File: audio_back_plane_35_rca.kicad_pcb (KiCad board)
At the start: 4 copper layers, 75 x 61 mm, 30 parts, among them SW3 SW1, U1 ESP32-DevKitC - DEVKIT, U3 Teensy 4.1 - DEVKIT

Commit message: update
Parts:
- added C1: 0.1uF, project_fp:C_0805_2012Metric_Pad1.15x1.40mm_HandSolder, F.Cu at (103.2, 104.7)
- added C2: 0.1uF, project_fp:C_0805_2012Metric_Pad1.15x1.40mm_HandSolder, F.Cu at (118.3, 130.1)
- added C8: 1uF, project_fp:C_0805_2012Metric_Pad1.15x1.40mm_HandSolder, F.Cu at (109.1, 129.9)
- added D3: SK6812_4020_SIDE_LED, project_fp:LED_4691, F.Cu at (107.2, 100.2)
- added D4: SK6812_4020_SIDE_LED, project_fp:LED_4691, F.Cu at (119.5, 100.2)
- added R1: 2.2k ohm - 2200 ohm, project_fp:R_0805_2012Metric_Pad1.20x1.40mm_HandSolder, F.Cu at (117.2, 125.1)
- D1, D2: value WS2812B - COM-16347 -> HEADER; footprint Connector_PinHeader_1.00mm:PinHeader_1x04_P1.00mm_Vertical -> project_fp:PinHeader_1x04_P1.00mm_Vertical_WS2812_LED_mod
- R10, R12, R13, R14, R17, R19, R20, R21, R6, R7, R8, R9: footprint Resistor_THT:R_Axial_DIN0204_L3.6mm_D1.6mm_P5.08mm_Horizontal -> project_fp:R_0805_2012Metric_Pad1.20x1.40mm_HandSolder
- SW3: value SW1 -> OS102011MA1QN1
- board_outline1: value board -> TAC5212 Module
- moved board_outline2 30.0 mm to (98.5, 146.7)
- moved G1 14.0 mm to (113.5, 130.1), turned to 0 degrees
- moved R12 7.47 mm to (134.9, 105.1)
- moved C3 4.54 mm to (109.0, 111.9), turned to -90 degrees
- moved C5 4.44 mm to (118.5, 111.9), turned to -90 degrees
- moved R8 3.54 mm to (134.3, 132.5)
- moved R19 3.16 mm to (164.5, 98.5)
- moved R20 3.16 mm to (161.4, 98.5)
- moved R21 3.16 mm to (158.2, 98.5)
- moved R14 2.54 mm to (134.9, 107.7)
- moved D2 2.30 mm to (118.0, 108.3)
- moved D1 2.20 mm to (106.0, 108.3)
- moved R17 1.55 mm to (116.2, 111.9), turned to -90 degrees
- moved R10 1.54 mm to (134.3, 127.7)
- moved R9 1.54 mm to (134.3, 130.1)
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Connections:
- HPTRS1 pad 2: Net-(board_outline1-OUTP) -> Net-(board_outline1-OUT2P)
- HPTRS1 pad 5: Net-(board_outline1-OUT2P) -> Net-(board_outline1-OUTP)
- HPTRS2 pad 2: Net-(board_outline1-IN1P) -> Net-(SW3-C)
- HPTRS2 pad 5: Net-(SW3-C) -> Net-(board_outline1-IN1P)
- MIC1 pad 2: unconnected-(MIC1-SELECT-Pad2) -> GND
- MIC2 pad 2: unconnected-(MIC2-SELECT-Pad2) -> 3.3V
- U1 pad 23: Net-(ILI1-CS) -> unconnected-(U1-*MTDO/GPIO15/ADC2_CH3-Pad23)
- U1 pad 24: Net-(ILI1-DC) -> unconnected-(U1-ADC2_CH2/*GPIO2-Pad24)
- U1 pad 26: Net-(ILI1-RESET) -> unconnected-(U1-ADC2_CH0/GPIO4-Pad26)
- U1 pad 30: Net-(ILI1-SCK) -> unconnected-(U1-GPIO18-Pad30)
- U1 pad 31: Net-(ILI1-T_DO(MISO)) -> unconnected-(U1-GPIO19-Pad31)
- U1 pad 33: /ESP32_IO21_SDA -> unconnected-(U1-GPIO21-Pad33)
- U1 pad 36: /ESP32_IO22_SCL -> unconnected-(U1-GPIO22-Pad36)
- U1 pad 37: Net-(ILI1-SDI(MOSI)) -> unconnected-(U1-GPIO23-Pad37)
- U1 pad 5: Net-(GPI1-Pin_2) -> unconnected-(U1-VDET_1/GPIO34/ADC1_CH6-Pad5)
- U1 pad 6: Net-(GPI1-Pin_1) -> unconnected-(U1-VDET_2/GPIO35/ADC1_CH7-Pad6)
- U1 pad 7: Net-(ILI1-T_CS) -> unconnected-(U1-32K_XP/GPIO32/ADC1_CH4-Pad7)
- U3 pad 16: T_BUTTON1 -> unconnected-(U3-24_A10_TX6_SCL2-Pad16)
- U3 pad 17: T_BUTTON2 -> unconnected-(U3-25_A11_RX6_SDA2-Pad17)
- U3 pad 2: MIDI_RX -> unconnected-(U3-0_RX1_CRX2_CS1-Pad2)
- U3 pad 26: 34_RX8_RESET2 -> unconnected-(U3-34_RX8-Pad26)
- U3 pad 3: MIDI_TX_T -> unconnected-(U3-1_TX1_CTX2_MISO1-Pad3)
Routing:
- net /OUTPUTA: track 108.0 -> 81.0 mm
- net Net-(board_outline1-OUT2P): track 49.6 -> 33.8 mm
- net /OUTPUTB: track 89.7 -> 74.1 mm, vias 1 -> 2
- net 5V: track 130.3 -> 144.1 mm, vias 1 -> 4
- net Net-(SW3-C): track 31.6 -> 18.7 mm
- net BCLK1: track 26.1 -> 34.6 mm
- net Net-(board_outline1-IN1P): track 24.9 -> 33.2 mm
- net 3.3V: track 125.6 -> 133.8 mm, vias 2 -> 5
- net Net-(D2-Pin_1): track 4.21 -> 12.2 mm, vias 0 -> 1
- net Net-(board_outline1-OUTP): track 39.6 -> 47.3 mm
- net ESP32_IO0: track 40.2 -> 47.5 mm
- net Net-(D1-Pin_1): track 4.20 -> 11.4 mm, vias 0 -> 1
- net ESP32_IO33_SPI_CS: track 24.5 -> 31.5 mm
- net USB_SHIELD2: track 27.0 -> 21.4 mm
- net HOST_5V: track 38.8 -> 43.1 mm
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
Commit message: update
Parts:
- removed C3, C5: 0.1uF, project_fp:C_0805_2012Metric_Pad1.15x1.40mm_HandSolder
- removed D1, D2: HEADER, project_fp:PinHeader_1x04_P1.00mm_Vertical_WS2812_LED_mod
- removed R13, R17: 470 ohm, project_fp:R_0805_2012Metric_Pad1.20x1.40mm_HandSolder
- removed S1: PEC12R-2220F-S0024, project_fp:XDCR_PEC12R-2220F-S0024
- added D10: SK6812, project_fp:LED_SK6812_EC15_1.5x1.5mm, B.Cu at (136.3, 130.9)
- added D11: SK6812, project_fp:LED_SK6812_EC15_1.5x1.5mm, B.Cu at (149.7, 90.9)
- added D5: SK6812, project_fp:LED_SK6812_EC15_1.5x1.5mm, B.Cu at (157.3, 130.7)
- added D6: SK6812, project_fp:LED_SK6812_EC15_1.5x1.5mm, B.Cu at (164.7, 131.1)
- added D7: SK6812, project_fp:LED_SK6812_EC15_1.5x1.5mm, B.Cu at (162.9, 90.5)
- added D8: SK6812, project_fp:LED_SK6812_EC15_1.5x1.5mm, B.Cu at (137.5, 91.1)
- added SW1: RotaryEncoder_Switch_MP, project_fp:RotaryEncoder_Alps_EC11E_Vertical_H20mm, B.Cu at (139.6, 125.4)
- added SW2: TL1105WF160Q - 3.15mm actuator, project_fp:Tactile_Switch_4.54.5MM, B.Cu at (166.3, 118.7)
- added SW4: TL1105WF160Q - 3.15mm actuator, project_fp:Tactile_Switch_4.54.5MM, B.Cu at (157.7, 118.7)
- added SW5: TL1105WF160Q - 3.15mm actuator, project_fp:Tactile_Switch_4.54.5MM, B.Cu at (107.3, 119.7)
- added SW6: TL1105WF160Q - 3.15mm actuator, project_fp:Tactile_Switch_4.54.5MM, B.Cu at (116.7, 119.9)
- D3, D4: value SK6812_4020_SIDE_LED -> SK6812; footprint project_fp:LED_4691 -> project_fp:LED_SK6812_EC15_1.5x1.5mm; moved to B.Cu
- moved D4 30.4 mm to (116.9, 130.5), turned to 0 degrees
- moved D3 30.3 mm to (106.9, 130.5), turned to 0 degrees
- moved R19 25.1 mm to (140.6, 106.3)
- moved R20 25.1 mm to (137.5, 106.3)
- moved R21 25.1 mm to (134.3, 106.3)
- moved MIC1 19.2 mm to (112.2, 100.9)
- moved C9 17.1 mm to (162.2, 107.3)
- moved MIC2 17.1 mm to (161.5, 103.3)
- moved C10 15.0 mm to (110.7, 108.1)
- moved HPTRS2 11.8 mm to (161.8, 85.6)
- moved SW3 8.00 mm to (170.9, 96.1)
- moved HPTRS1 0.76 mm to (137.2, 85.8)
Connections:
- D3 pad 1: Net-(D1-Pin_1) -> 5V
- D3 pad 2: 5V -> Net-(D3-DOUT)
- D3 pad 3: unconnected-(D3-DOUT-Pad3) -> GND
- D3 pad 4: GND -> Net-(D1-Pin_1)
- D4 pad 1: Net-(D2-Pin_1) -> 5V
- D4 pad 2: 5V -> Net-(D4-DOUT)
- D4 pad 3: unconnected-(D4-DOUT-Pad3) -> GND
- D4 pad 4: GND -> Net-(D2-Pin_1)
- U3 pad 16: unconnected-(U3-24_A10_TX6_SCL2-Pad16) -> T_BUTTON1
- U3 pad 17: unconnected-(U3-25_A11_RX6_SDA2-Pad17) -> T_BUTTON2
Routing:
- net GND: track 23.9 -> 34.4 mm
- net /OUTPUTB: track 74.1 -> 63.6 mm
- net Net-(D2-Pin_1): track 12.2 -> 3.32 mm, vias 1 -> 0
- net 5V: track 144.1 -> 153.0 mm, vias 4 -> 5
- net 3.3V: track 133.8 -> 129.1 mm
- net T_BUTTON1: track 0.00 -> 2.84 mm
- net T_BUTTON2: track 0.00 -> 1.84 mm
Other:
- board text added: "< VOL >"
- board text added: "BT WIFI"
- board text added: "INPUT"
- board text added: "MIC"
- board text added: "NEXT"
- board text added: "PHONES"
- board text added: "PLAY PAUSE STOP"
- board text added: "PREV"
- board text added: "SELECT MODE"

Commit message: update
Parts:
- added C3: 0.1uF, project_fp:C_0805_2012Metric_Pad1.15x1.40mm_HandSolder, F.Cu at (189.4, 161.0)
- added C5: 0.1uF, project_fp:C_0805_2012Metric_Pad1.15x1.40mm_HandSolder, F.Cu at (189.4, 163.9)
- added D1: HEADER, project_fp:PinHeader_1x04_P1.00mm_Vertical_WS2812_LED_mod, F.Cu at (188.8, 179.4)
- added D2: HEADER, project_fp:PinHeader_1x04_P1.00mm_Vertical_WS2812_LED_mod, F.Cu at (192.1, 179.4)
- added D9: SK6812, project_fp:LED_SK6812, F.Cu at (191.6, 174.6)
- added R13: 470 ohm, project_fp:R_0805_2012Metric_Pad1.20x1.40mm_HandSolder, F.Cu at (189.4, 166.9)
- added R17: 470 ohm, project_fp:R_0805_2012Metric_Pad1.20x1.40mm_HandSolder, F.Cu at (189.4, 169.8)
- added REF**: SW_Push_1P1T_NO_6x6mm_H9.5mm, Button_Switch_SMD:SW_Push_1P1T_NO_6x6mm_H9.5mm, F.Cu at (196.7, 99.9)
- added S1: PEC12R-2220F-S0024, project_fp:XDCR_PEC12R-2220F-S0024, F.Cu at (178.1, 167.1)
- added SW7: TL1105WF160Q - 3.15mm actuator, project_fp:Tactile_Switch_4.54.5MM, B.Cu at (111.1, 95.1)
- D10: moved to F.Cu
- moved board_outline2 104.1 mm to (178.7, 80.4), turned to 180 degrees
- moved board_outline1 95.4 mm to (103.9, 80.8), turned to -90 degrees
- moved USBA1 83.8 mm to (164.5, 80.6), turned to 180 degrees
- moved U1 81.9 mm to (177.2, 127.2), turned to 180 degrees
- moved SW3 73.4 mm to (106.3, 131.0), turned to -90 degrees
- moved C1 72.9 mm to (174.0, 122.4), turned to 90 degrees
- moved HPTRS2 72.6 mm to (115.4, 141.4), turned to 90 degrees
- moved D3 70.7 mm to (170.3, 99.3), turned to 180 degrees
- moved C8 67.5 mm to (168.1, 97.2), turned to 0 degrees
- moved D4 67.3 mm to (165.5, 83.9), turned to 180 degrees
- moved D7 66.9 mm to (114.3, 136.6), turned to 0 degrees
- moved D10 66.0 mm to (193.3, 164.1), turned to 0 degrees
- moved SW5 63.8 mm to (169.9, 107.4), turned to -90 degrees
- moved G1 60.2 mm to (163.7, 97.0), turned to 180 degrees
- moved D6 59.7 mm to (117.5, 94.5), turned to 0 degrees
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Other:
- board text added: "PLAY REC"
- board text added: "SD"
- board text added: "USB"

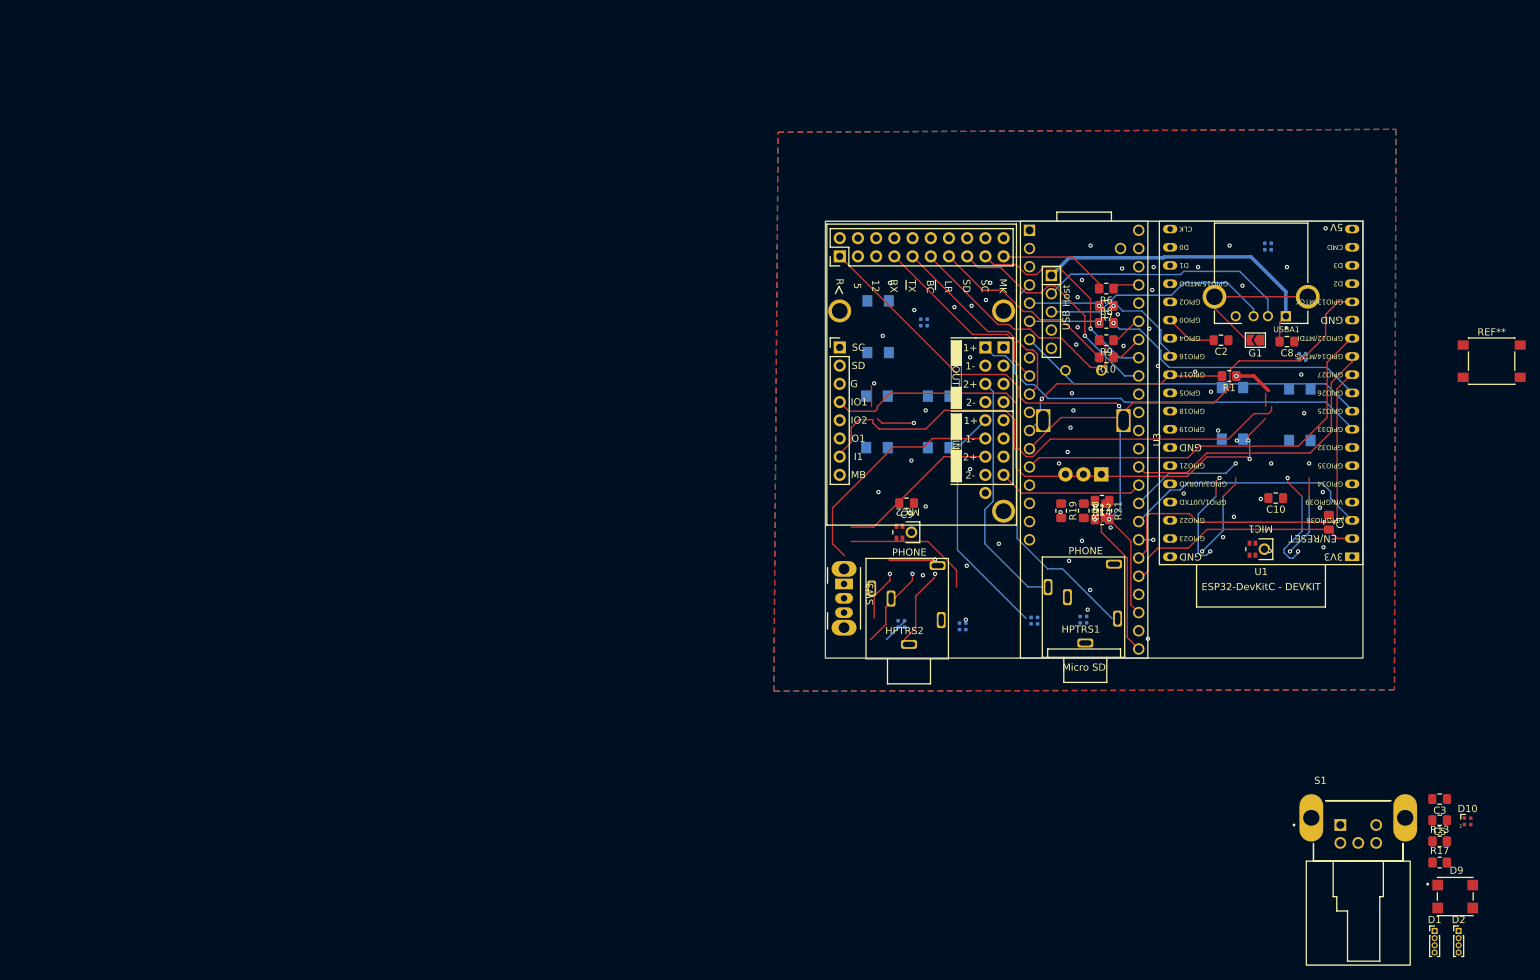
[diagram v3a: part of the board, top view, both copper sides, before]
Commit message: added tft touchscreen
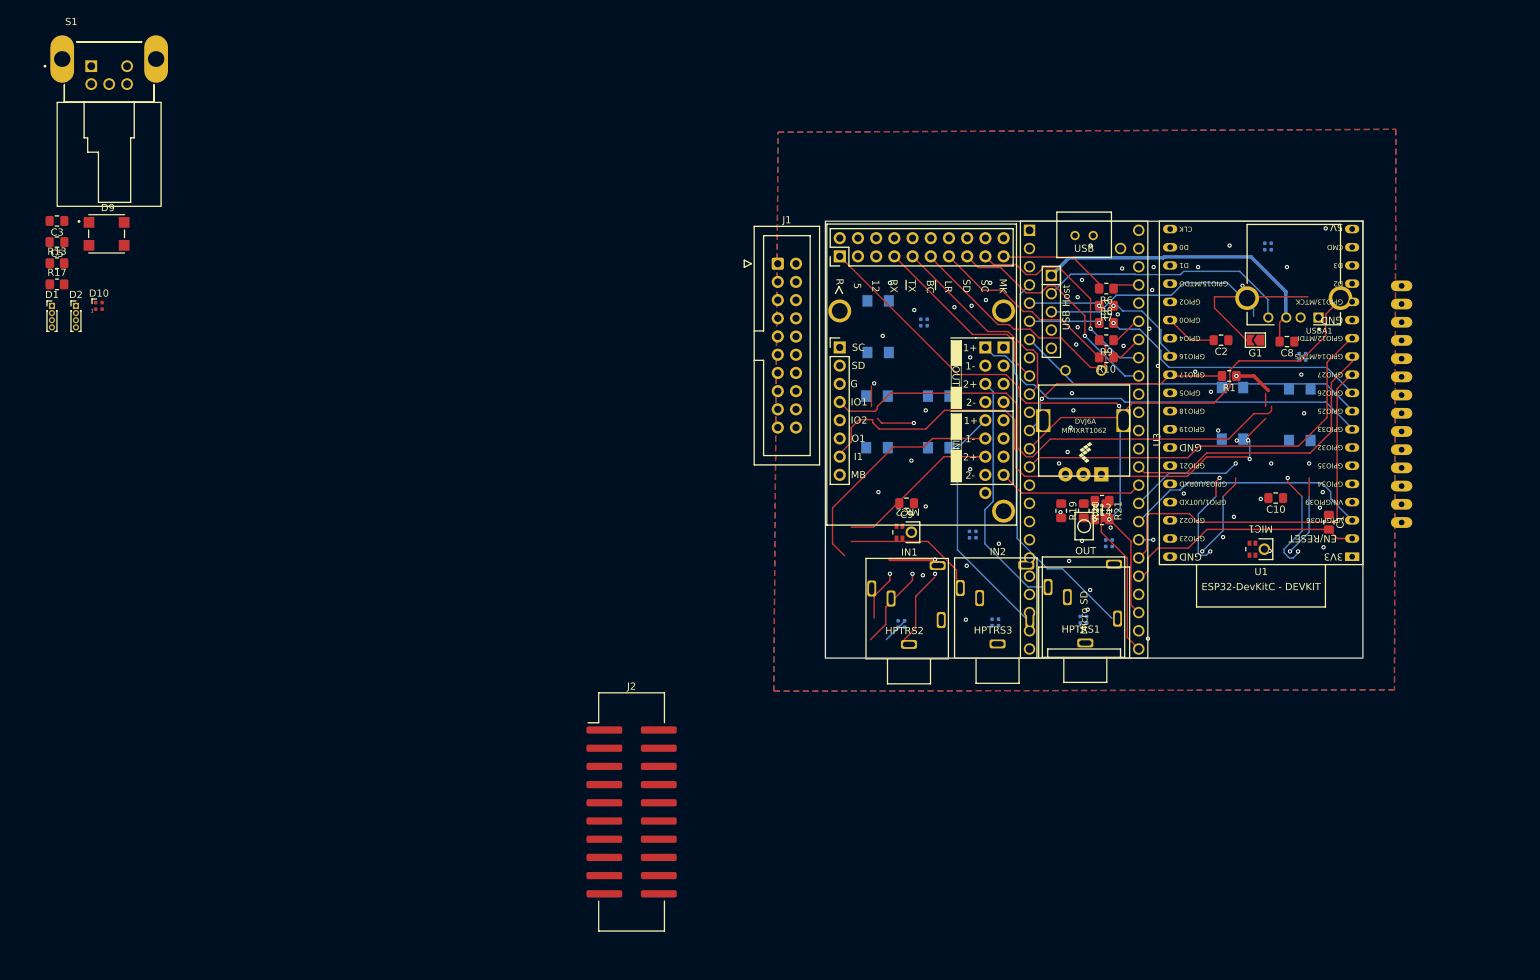
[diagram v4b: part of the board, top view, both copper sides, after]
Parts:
- removed REF**: SW_Push_1P1T_NO_6x6mm_H9.5mm, Button_Switch_SMD:SW_Push_1P1T_NO_6x6mm_H9.5mm
- removed SW3: OS102011MA1QN1, Button_Switch_THT:SW_Slide_SPDT_Angled_CK_OS102011MA1Q
- added D12: SK6812, project_fp:LED_SK6812_EC15_1.5x1.5mm, B.Cu at (143.3, 125.3)
- added HPTRS3: 3.5MM JACK, project_fp:35RAPC3BH3, F.Cu at (127.8, 141.3)
- added J1: Conn_02x10_Odd_Even, Connector_IDC:IDC-Header_2x10_P2.54mm_Vertical, F.Cu at (97.1, 86.3)
- added J2: Conn_02x10_Odd_Even, Connector_IDC:IDC-Header_2x10_P2.54mm_Vertical_SMD, F.Cu at (76.7, 162.8)
- added U2: TFT_320x240, project_fp:TFT-320x240, B.Cu at (184.1, 105.9)
- U3: footprint project_fp:Teensy41_mod2 -> project_fp:Teensy41_mod
- moved D1 211.7 mm to (-4.17, 92.2)
- moved D2 211.7 mm to (-0.82, 92.2)
- moved D9 209.7 mm to (3.45, 82.1)
- moved C3 209.1 mm to (-3.48, 80.3)
- moved C5 209.1 mm to (-3.48, 83.3)
- moved R13 209.1 mm to (-3.48, 86.2)
- moved R17 209.1 mm to (-3.48, 89.2)
- moved D10 204.1 mm to (2.38, 92.2)
- moved S1 203.9 mm to (3.81, 61.2)
- moved D5 14.8 mm to (124.3, 124.1)
- moved D11 4.58 mm to (127.5, 136.3)
- moved USBA1 4.56 mm to (169.1, 80.8)
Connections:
- HPTRS2 pad 2: Net-(SW3-C) -> Net-(board_outline1-IN1M)
- board_outline1 pad 31: Net-(SW3-B) -> Net-(board_outline1-IN1M)
- board_outline1 pad 35: unconnected-(board_outline1-IN2M-Pad35) -> Net-(board_outline1-IN2M)
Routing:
- net Net-(board_outline1-IN1M): track 0.00 -> 32.7 mm
- net Net-(SW3-B): track 32.7 -> 0.00 mm
- net 3.3V: track 129.1 -> 151.9 mm
- net Net-(board_outline1-IN2P): track 22.8 -> 0.00 mm
- net Net-(SW3-C): track 18.7 -> 0.00 mm
- net (no net): track 0.00 -> 18.7 mm
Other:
- board text added: "IN1"
- board text added: "IN2"
- board text added: "OUT1"
- board text added: "PLAY/PAUSE"
- board text removed: "INPUT"
- board text removed: "PHONES"
- board text removed: "PLAY PAUSE STOP"

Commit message: update
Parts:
- removed J1: Conn_02x10_Odd_Even, Connector_IDC:IDC-Header_2x10_P2.54mm_Vertical
- removed J2: Conn_02x10_Odd_Even, Connector_IDC:IDC-Header_2x10_P2.54mm_Vertical_SMD
- removed the U2 at (184.1, 105.9)
- added HPTRS2: 3.5MM JACK, project_fp:35RAPC3BH3, F.Cu at (128.0, 140.9)
- added IC1: TMUX4053DYYR, SamacSys_Parts:SOP50P326X110-16N, F.Cu at (100.9, 122.9)
- added IC2: SN74LVC245ARGYR, SamacSys_Parts:SN74LVC541ARGYR, F.Cu at (58.1, 112.5)
- added J3: header, project_fp:PinHeader_1x02_P2.54mm_Vertical_W_CUT, F.Cu at (18.4, 158.8)
- added J4: header, project_fp:PinHeader_1x02_P2.54mm_Vertical_W_CUT, F.Cu at (24.0, 158.8)
- added R16: 0 ohm, project_fp:R_0805_2012Metric_Pad1.20x1.40mm_HandSolder, F.Cu at (17.0, 152.5)
- added R17: 0 ohm, project_fp:R_0805_2012Metric_Pad1.20x1.40mm_HandSolder, F.Cu at (17.0, 155.4)
- added R18: 49.9 ohm, project_fp:R_0805_2012Metric_Pad1.20x1.40mm_HandSolder, F.Cu at (21.8, 146.6)
- added R19: 49.9 ohm, project_fp:R_0805_2012Metric_Pad1.20x1.40mm_HandSolder, F.Cu at (21.8, 149.5)
- added R20: 49.9 ohm, project_fp:R_0805_2012Metric_Pad1.20x1.40mm_HandSolder, F.Cu at (21.8, 152.5)
- added R21: 49.9 ohm, project_fp:R_0805_2012Metric_Pad1.20x1.40mm_HandSolder, F.Cu at (21.8, 155.4)
- added R22: 49.9 ohm, project_fp:R_0805_2012Metric_Pad1.20x1.40mm_HandSolder, F.Cu at (26.5, 146.6)
- added R23: 49.9 ohm, project_fp:R_0805_2012Metric_Pad1.20x1.40mm_HandSolder, F.Cu at (26.5, 149.5)
- added R24: 49.9 ohm, project_fp:R_0805_2012Metric_Pad1.20x1.40mm_HandSolder, F.Cu at (26.5, 152.5)
- added R25: 49.9 ohm, project_fp:R_0805_2012Metric_Pad1.20x1.40mm_HandSolder, F.Cu at (26.5, 155.4)
- added R6: 10k, project_fp:R_0805_2012Metric_Pad1.20x1.40mm_HandSolder, F.Cu at (17.0, 146.6)
- added R9: 100 ohm, project_fp:R_0805_2012Metric_Pad1.20x1.40mm_HandSolder, F.Cu at (17.0, 149.5)
- added TDM1: header, project_fp:T-DSP_Expansion_Header_2x10_ALT_GND, F.Cu at (-5.33, 138.6)
- added TDM2: header, project_fp:T-DSP_Expansion_Header_2x10_ALT_GND, F.Cu at (7.91, 138.6)
- U1: renamed from U3; footprint project_fp:Teensy41_mod -> project_fp:Teensy41_mod2
- board_outline2: footprint project_fp:audio_project_board_outline_60.96x45 -> project_fp:audio_project_board_outline_60.96x100
- moved C2 23.8 mm to (93.9, 130.6)
- moved MIC2 23.8 mm to (94.6, 134.7)
- moved MIC1 19.7 mm to (182.9, 134.4), turned to 90 degrees
- moved HPTRS3 12.6 mm to (102.8, 141.1)
- moved HPTRS4 12.2 mm to (115.6, 141.1)
- moved board_outline2 11.0 mm to (189.7, 80.5)
- renumbered C3 to C1, C9 to C2, C5 to C3, C1 to C4, C10 to C5, C2 to C6, C8 to C7, D12 to D10, D9 to D12, D3 to D2, D6 to D3, D2 to D4, D4 to D5, D5 to D6, D10 to D9, HPTRS2 to HPTRS3, HPTRS3 to HPTRS4, R6 to R1, R14 to R10, R17 to R11, R1 to R12, R19 to R13, R20 to R14, R21 to R15, R7 to R2, R8 to R3, R9 to R4, R10 to R5, R13 to R7, R12 to R8, SW4 to SW3, SW7 to SW4, U1 to U2
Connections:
- HPTRS1 pad 2: Net-(board_outline1-OUT2P) -> Net-(IC1-D1)
- HPTRS4 pad 4: unconnected-(HPTRS3-Pad4) (its old number) -> IN2_JACK_DETECT
- U1 pad 18: unconnected-(U3-26_A12_MOSI1-Pad18) -> IN2_JACK_DETECT
- U2 pad 23: unconnected-(U1-*MTDO/GPIO15/ADC2_CH3-Pad23) -> Net-(U2-*MTDO/GPIO15/ADC2_CH3)
- U2 pad 24: unconnected-(U1-ADC2_CH2/*GPIO2-Pad24) -> Net-(U2-ADC2_CH2/*GPIO2)
- U2 pad 26: unconnected-(U1-ADC2_CH0/GPIO4-Pad26) -> Net-(U2-ADC2_CH0/GPIO4)
- U2 pad 30: unconnected-(U1-GPIO18-Pad30) -> Net-(U2-GPIO18)
- U2 pad 31: unconnected-(U1-GPIO19-Pad31) -> Net-(U2-GPIO19)
- U2 pad 37: unconnected-(U1-GPIO23-Pad37) -> Net-(U2-GPIO23)
- U2 pad 7: unconnected-(U1-32K_XP/GPIO32/ADC1_CH4-Pad7) -> Net-(U2-32K_XP/GPIO32/ADC1_CH4)
- board_outline1 pad 23: unconnected-(board_outline1-OUT1M-Pad23) -> Net-(IC1-S1A)
- board_outline1 pad 25: Net-(board_outline1-OUT2P) -> Net-(IC1-S1B)
- board_outline1 pad 27: unconnected-(board_outline1-OUT2M-Pad27) -> Net-(IC1-S3B)
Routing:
- net Net-(board_outline1-OUT2P): track 33.8 -> 0.00 mm
- net Net-(IC1-S1B): track 0.00 -> 33.8 mm
- net (no net): track 18.7 -> 45.3 mm
- net Net-(U1-33_MCLK2): track 23.3 -> 0.00 mm
- net 3.3V: track 151.9 -> 129.1 mm
- net Net-(board_outline1-IN2P): track 0.00 -> 22.8 mm
- net Net-(D4-Pin_1): track 3.32 -> 0.00 mm
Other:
- board size 75 x 61 mm -> 100 x 61 mm
